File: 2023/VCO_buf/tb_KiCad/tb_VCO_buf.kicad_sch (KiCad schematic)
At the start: 2 parts

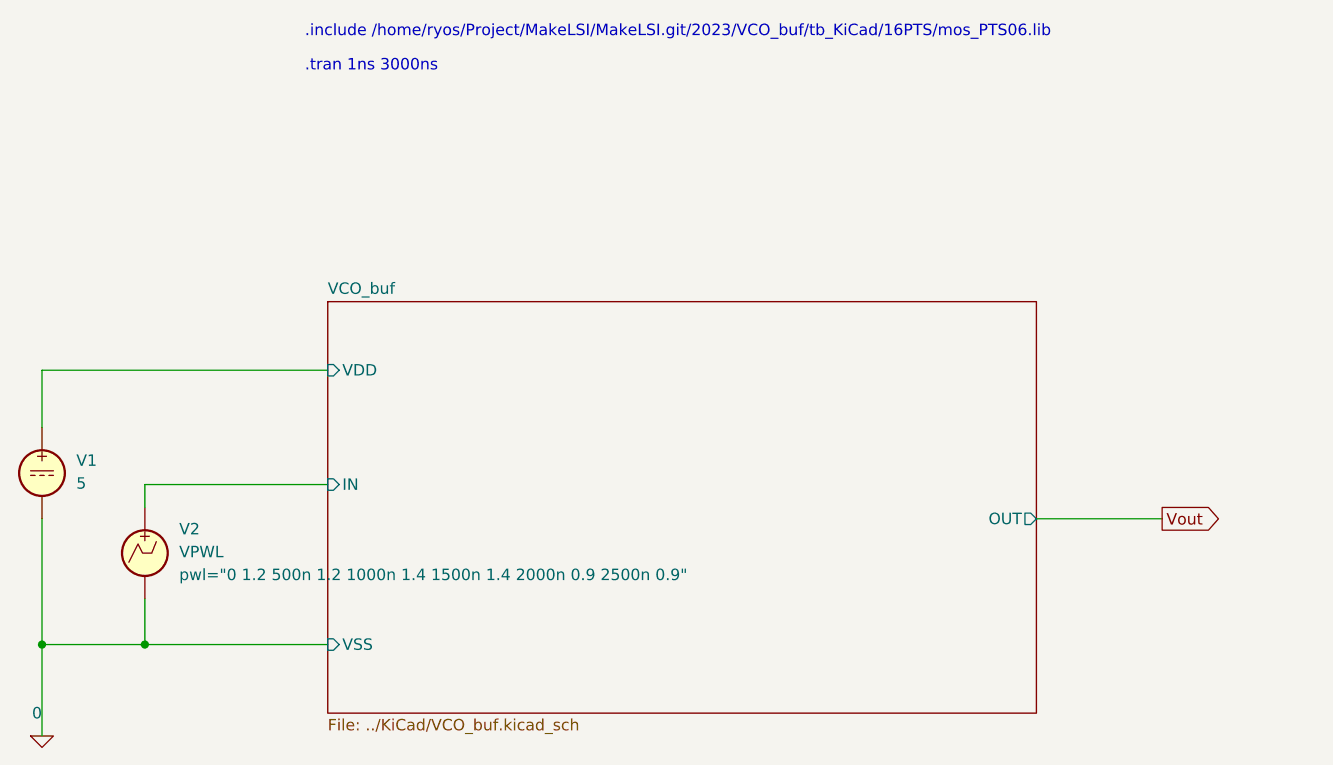
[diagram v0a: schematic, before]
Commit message: 最後に２つバッファつけて LVS OK.
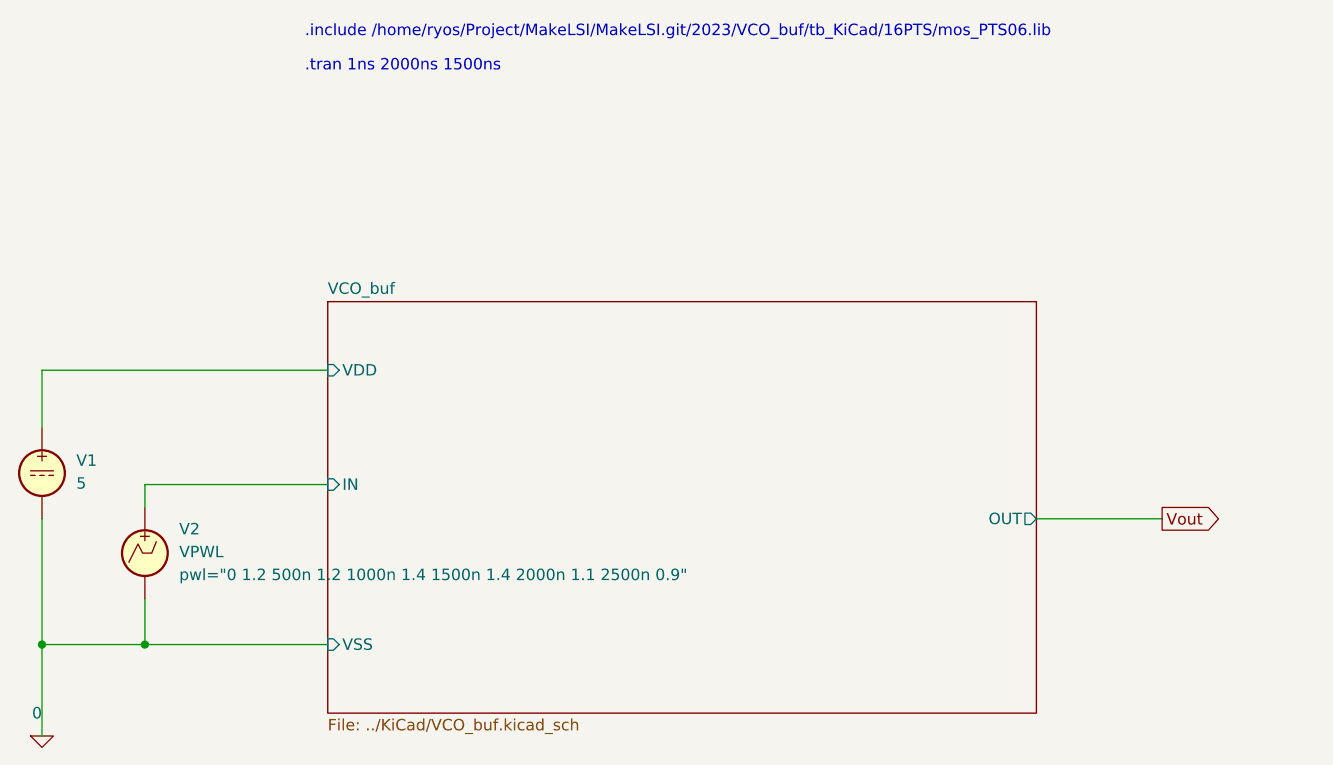
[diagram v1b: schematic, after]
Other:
- note added: ".tran 1ns 2000ns 1500ns"
- note removed: ".tran 1ns 3000ns"
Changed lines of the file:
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@@
     (effects (font (size 1.27 1.27)) (justify left bottom))
   )
-  (text ".tran 1ns 3000ns\n" (at 85.09 30.48 0)
+  (text ".tran 1ns 2000ns 1500ns\n" (at 85.09 30.48 0)
     (effects (font (size 1.27 1.27)) (justify left bottom))
   )
@@
       (effects (font (size 1.27 1.27)) (justify left) hide)
     )
-    (property "Sim.Params" "pwl=\"0 1.2 500n 1.2 1000n 1.4 1500n 1.4 2000n 0.9 2500n 0.9\"" (at 71.12 86.2302 0)
+    (property "Sim.Params" "pwl=\"0 1.2 500n 1.2 1000n 1.4 1500n 1.4 2000n 1.1 2500n 0.9\"" (at 71.12 86.2302 0)
       (effects (font (size 1.27 1.27)) (justify left))
     )

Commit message: とりあえず今となっては必要のないファイルも含めてコミット。
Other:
- note added: ".tran 1ns 2000ns 1400ns"
- note removed: ".tran 1ns 2000ns 1500ns"
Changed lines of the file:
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@@
     (effects (font (size 1.27 1.27)) (justify left bottom))
   )
-  (text ".tran 1ns 2000ns 1500ns\n" (at 85.09 30.48 0)
+  (text ".tran 1ns 2000ns 1400ns\n" (at 85.09 30.48 0)
     (effects (font (size 1.27 1.27)) (justify left bottom))
   )
@@
       (effects (font (size 1.27 1.27)) (justify left) hide)
     )
-    (property "Sim.Params" "pwl=\"0 1.2 500n 1.2 1000n 1.4 1500n 1.4 2000n 1.1 2500n 0.9\"" (at 71.12 86.2302 0)
+    (property "Sim.Params" "pwl=\"0 1.2 500n 1.2 1000n 1.4 1500n 1.4 2000n 1.1 2500n 0.5\"" (at 71.12 86.2302 0)
       (effects (font (size 1.27 1.27)) (justify left))
     )
